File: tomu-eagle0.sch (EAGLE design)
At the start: 21 parts, among them U1 EFM32HG309F64G, X1 USBPCB

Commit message: added first pass at touch sensors
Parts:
- removed 0A, 0B, 1A, 1B: TPTP08R, testpad:TPTP08R
- removed X1: USBPCB, usb:USBPCB
- added U$1: USBPCB2, todstuff:USBPCB2
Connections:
- net CAP0A: no longer 0A.TP
- net CAP0B: no longer 0B.TP
- net CAP1A: no longer 1A.TP
- net CAP1B: no longer 1B.TP
- net GND: now also U$1.GND; no longer X1.GND
- net USB_D+: now also U$1.D+; no longer X1.D+
- net USB_D-: now also U$1.D-; no longer X1.D-
- net VUSB: now also U$1.VBUS; no longer X1.VBUS

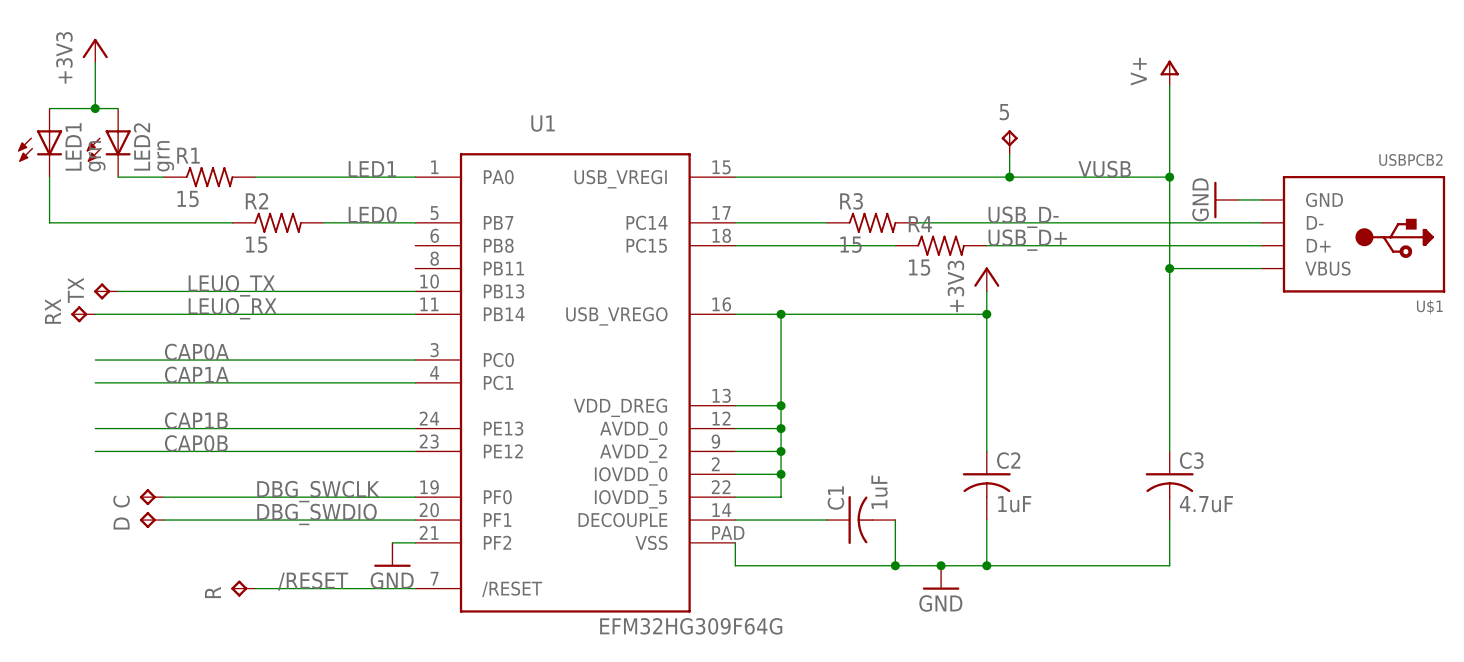
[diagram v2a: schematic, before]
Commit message: sigh. QFN24 is 5x5 not 4x4
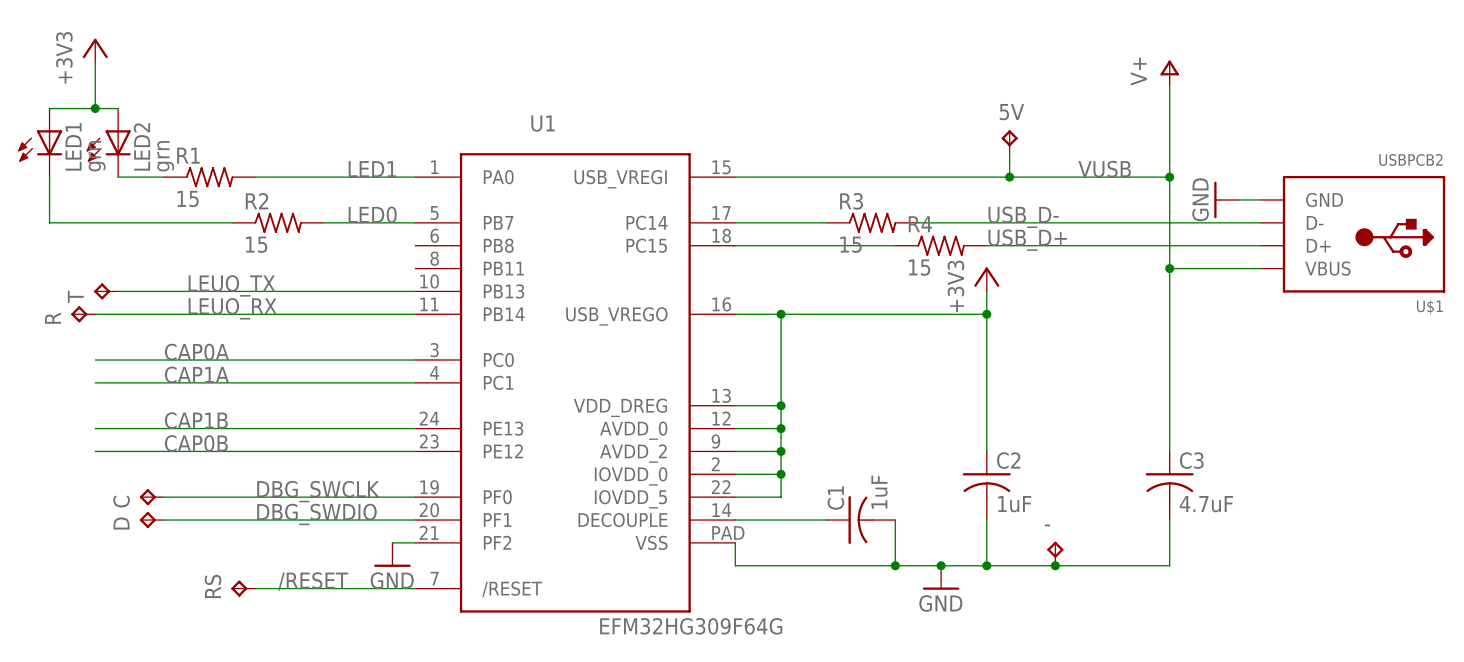
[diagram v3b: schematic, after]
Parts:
- removed RX, TX: TPTP08R, testpad:TPTP08R
- added -: TPTP10SQ, testpad:TPTP10SQ
- added RS, T: TPTP10R, testpad:TPTP10R
- C, D, R: value TPTP08R -> TPTP10R; device testpad:TPTP08R -> testpad:TPTP10R
- renumbered 5 to 5V
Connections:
- net /RESET: now also RS.TP; no longer R.TP
- net GND: now also -.TP
- net LEUO_RX: now also R.TP; no longer RX.TP
- net LEUO_TX: now also T.TP; no longer TX.TP
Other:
- moved on the sheet: R
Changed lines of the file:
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@@
 <part name="LED1" library="adafruit" library_urn="urn:adsk.eagle:library:420" deviceset="LED" device="CHIP-LED0603" value="grn"/>
 <part name="LED2" library="adafruit" library_urn="urn:adsk.eagle:library:420" deviceset="LED" device="CHIP-LED0603" value="grn"/>
-<part name="TX" library="testpad" library_urn="urn:adsk.eagle:library:385" deviceset="TP" device="TP08R" package3d_urn="urn:adsk.eagle:package:27956/1"/>
-<part name="RX" library="testpad" library_urn="urn:adsk.eagle:library:385" deviceset="TP" device="TP08R" package3d_urn="urn:adsk.eagle:package:27956/1"/>
-<part name="D" library="testpad" library_urn="urn:adsk.eagle:library:385" deviceset="TP" device="TP08R" package3d_urn="urn:adsk.eagle:package:27956/1"/>
-<part name="C" library="testpad" library_urn="urn:adsk.eagle:library:385" deviceset="TP" device="TP08R" package3d_urn="urn:adsk.eagle:package:27956/1"/>
-<part name="R" library="testpad" library_urn="urn:adsk.eagle:library:385" deviceset="TP" device="TP08R" package3d_urn="urn:adsk.eagle:package:27956/1"/>
+<part name="T" library="testpad" library_urn="urn:adsk.eagle:library:385" deviceset="TP" device="TP10R" package3d_urn="urn:adsk.eagle:package:27959/1" value="TPTP10R"/>
+<part name="R" library="testpad" library_urn="urn:adsk.eagle:library:385" deviceset="TP" device="TP10R" package3d_urn="urn:adsk.eagle:package:27959/1" value="TPTP10R"/>
+<part name="D" library="testpad" library_urn="urn:adsk.eagle:library:385" deviceset="TP" device="TP10R" package3d_urn="urn:adsk.eagle:package:27959/1" value="TPTP10R"/>
+<part name="C" library="testpad" library_urn="urn:adsk.eagle:library:385" deviceset="TP" device="TP10R" package3d_urn="urn:adsk.eagle:package:27959/1" value="TPTP10R"/>
+<part name="RS" library="testpad" library_urn="urn:adsk.eagle:library:385" deviceset="TP" device="TP10R" package3d_urn="urn:adsk.eagle:package:27959/1" value="TPTP10R"/>
 <part name="GND1" library="supply1" library_urn="urn:adsk.eagle:library:371" deviceset="GND" device=""/>
-<part name="5" library="testpad" library_urn="urn:adsk.eagle:library:385" deviceset="TP" device="TP08R" package3d_urn="urn:adsk.eagle:package:27956/1"/>
+<part name="5V" library="testpad" library_urn="urn:adsk.eagle:library:385" deviceset="TP" device="TP08R" package3d_urn="urn:adsk.eagle:package:27956/1"/>
 <part name="U$1" library="todstuff" deviceset="USB" device="PCB2"/>
+<part name="-" library="testpad" library_urn="urn:adsk.eagle:library:385" deviceset="TP" device="TP10SQ" package3d_urn="urn:adsk.eagle:package:27962/1" value="TPTP10SQ"/>
 </parts>
 <sheets>
@@
 <instance part="LED1" gate="G$1" x="12.7" y="76.2"/>
 <instance part="LED2" gate="G$1" x="20.32" y="76.2"/>
-<instance part="TX" gate="G$1" x="17.78" y="58.42" rot="R90"/>
-<instance part="RX" gate="G$1" x="15.24" y="55.88" rot="R90"/>
+<instance part="T" gate="G$1" x="17.78" y="58.42" rot="R90"/>
+<instance part="R" gate="G$1" x="15.24" y="55.88" rot="R90"/>
 <instance part="D" gate="G$1" x="22.86" y="33.02" rot="R90"/>
 <instance part="C" gate="G$1" x="22.86" y="35.56" rot="R90"/>
-<instance part="R" gate="G$1" x="33.02" y="25.4" rot="R90"/>
+<instance part="RS" gate="G$1" x="33.02" y="25.4" rot="R90"/>
 <instance part="GND1" gate="1" x="50.8" y="27.94"/>
-<instance part="5" gate="G$1" x="119.38" y="76.2"/>
+<instance part="5V" gate="G$1" x="119.38" y="76.2"/>
 <instance part="U$1" gate="G$1" x="154.94" y="63.5" rot="R180"/>
+<instance part="-" gate="G$1" x="124.46" y="30.48"/>
 </instances>
 <busses>
@@
 <pinref part="C2" gate="G$1" pin="2"/>
 <wire x1="116.84" y1="27.94" x2="116.84" y2="33.02" width="0.1524" layer="91"/>
-<wire x1="116.84" y1="27.94" x2="137.16" y2="27.94" width="0.1524" layer="91"/>
+<wire x1="116.84" y1="27.94" x2="124.46" y2="27.94" width="0.1524" layer="91"/>
 <junction x="116.84" y="27.94"/>
 <pinref part="C3" gate="G$1" pin="2"/>
+<wire x1="124.46" y1="27.94" x2="137.16" y2="27.94" width="0.1524" layer="91"/>
 <wire x1="137.16" y1="27.94" x2="137.16" y2="33.02" width="0.1524" layer="91"/>
+<pinref part="-" gate="G$1" pin="TP"/>
+<junction x="124.46" y="27.94"/>
 </segment>
 <segment>
@@
 <junction x="137.16" y="71.12"/>
 <label x="127" y="71.12" size="1.778" layer="95"/>
-<pinref part="5" gate="G$1" pin="TP"/>
+<pinref part="5V" gate="G$1" pin="TP"/>
 <wire x1="119.38" y1="71.12" x2="137.16" y2="71.12" width="0.1524" layer="91"/>
 <wire x1="119.38" y1="73.66" x2="119.38" y2="71.12" width="0.1524" layer="91"/>
@@
 <pinref part="U1" gate="G$1" pin="PB13"/>
 <wire x1="53.34" y1="58.42" x2="20.32" y2="58.42" width="0.1524" layer="91"/>
-<pinref part="TX" gate="G$1" pin="TP"/>
+<pinref part="T" gate="G$1" pin="TP"/>
 <label x="27.94" y="58.42" size="1.778" layer="95"/>
 </segment>
@@
 <pinref part="U1" gate="G$1" pin="PB14"/>
 <wire x1="53.34" y1="55.88" x2="17.78" y2="55.88" width="0.1524" layer="91"/>
-<pinref part="RX" gate="G$1" pin="TP"/>
+<pinref part="R" gate="G$1" pin="TP"/>
 <label x="27.94" y="55.88" size="1.778" layer="95"/>
 </segment>
@@
 <wire x1="53.34" y1="25.4" x2="35.56" y2="25.4" width="0.1524" layer="91"/>
 <label x="38.1" y="25.4" size="1.778" layer="95"/>
-<pinref part="R" gate="G$1" pin="TP"/>
-</segment>
-</net>
+<pinref part="RS" gate="G$1" pin="TP"/>
+</segment>
+</net>

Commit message: more fixes
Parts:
- 5V: value TPTP08R -> TPTP10R; device testpad:TPTP08R -> testpad:TPTP10R
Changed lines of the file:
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@@
 <?xml version="1.0" encoding="utf-8"?>
 <!DOCTYPE eagle SYSTEM "eagle.dtd">
-<eagle version="8.5.2">
+<eagle version="8.6.0">
 <drawing>
 <settings>
@@
 <grid distance="0.1" unitdist="inch" unit="inch" style="lines" multiple="1" display="no" altdistance="0.01" altunitdist="inch" altunit="inch"/>
 <layers>
-<layer number="1" name="Top" color="4" fill="1" visible="no" active="no"/>
-<layer number="2" name="Route2" color="1" fill="3" visible="no" active="no"/>
-<layer number="3" name="Route3" color="4" fill="3" visible="no" active="no"/>
-<layer number="4" name="Route4" color="1" fill="4" visible="no" active="no"/>
-<layer number="5" name="Route5" color="4" fill="4" visible="no" active="no"/>
-<layer number="6" name="Route6" color="1" fill="8" visible="no" active="no"/>
-<layer number="7" name="Route7" color="4" fill="8" visible="no" active="no"/>
-<layer number="8" name="Route8" color="1" fill="2" visible="no" active="no"/>
-<layer number="9" name="Route9" color="4" fill="2" visible="no" active="no"/>
-<layer number="10" name="Route10" color="1" fill="7" visible="no" active="no"/>
-<layer number="11" name="Route11" color="4" fill="7" visible="no" active="no"/>
-<layer number="12" name="Route12" color="1" fill="5" visible="no" active="no"/>
-<layer number="13" name="Route13" color="4" fill="5" visible="no" active="no"/>
-<layer number="14" name="Route14" color="1" fill="6" visible="no" active="no"/>
-<layer number="15" name="Route15" color="4" fill="6" visible="no" active="no"/>
-<layer number="16" name="Bottom" color="3" fill="1" visible="no" active="no"/>
-<layer number="17" name="Pads" color="2" fill="1" visible="no" active="no"/>
-<layer number="18" name="Vias" color="2" fill="1" visible="no" active="no"/>
-<layer number="19" name="Unrouted" color="6" fill="1" visible="no" active="no"/>
-<layer number="20" name="Dimension" color="15" fill="1" visible="no" active="no"/>
-<layer number="21" name="tPlace" color="7" fill="1" visible="no" active="no"/>
-<layer number="22" name="bPlace" color="7" fill="1" visible="no" active="no"/>
-<layer number="23" name="tOrigins" color="15" fill="1" visible="no" active="no"/>
-<layer number="24" name="bOrigins" color="15" fill="1" visible="no" active="no"/>
-<layer number="25" name="tNames" color="7" fill="1" visible="no" active="no"/>
-<layer number="26" name="bNames" color="7" fill="1" visible="no" active="no"/>
-<layer number="27" name="tValues" color="7" fill="1" visible="no" active="no"/>
-<layer number="28" name="bValues" color="7" fill="1" visible="no" active="no"/>
+<layer number="1" name="Top" color="4" fill="1" visible="yes" active="no"/>
+<layer number="2" name="Route2" color="1" fill="3" visible="yes" active="no"/>
+<layer number="3" name="Route3" color="4" fill="3" visible="yes" active="no"/>
+<layer number="4" name="Route4" color="1" fill="4" visible="yes" active="no"/>
+<layer number="5" name="Route5" color="4" fill="4" visible="yes" active="no"/>
+<layer number="6" name="Route6" color="1" fill="8" visible="yes" active="no"/>
+<layer number="7" name="Route7" color="4" fill="8" visible="yes" active="no"/>
+<layer number="8" name="Route8" color="1" fill="2" visible="yes" active="no"/>
+<layer number="9" name="Route9" color="4" fill="2" visible="yes" active="no"/>
+<layer number="10" name="Route10" color="1" fill="7" visible="yes" active="no"/>
+<layer number="11" name="Route11" color="4" fill="7" visible="yes" active="no"/>
+<layer number="12" name="Route12" color="1" fill="5" visible="yes" active="no"/>
+<layer number="13" name="Route13" color="4" fill="5" visible="yes" active="no"/>
+<layer number="14" name="Route14" color="1" fill="6" visible="yes" active="no"/>
+<layer number="15" name="Route15" color="4" fill="6" visible="yes" active="no"/>
+<layer number="16" name="Bottom" color="3" fill="1" visible="yes" active="no"/>
+<layer number="17" name="Pads" color="2" fill="1" visible="yes" active="no"/>
+<layer number="18" name="Vias" color="2" fill="1" visible="yes" active="no"/>
+<layer number="19" name="Unrouted" color="6" fill="1" visible="yes" active="no"/>
+<layer number="20" name="Dimension" color="15" fill="1" visible="yes" active="no"/>
+<layer number="21" name="tPlace" color="7" fill="1" visible="yes" active="no"/>
+<layer number="22" name="bPlace" color="7" fill="1" visible="yes" active="no"/>
+<layer number="23" name="tOrigins" color="15" fill="1" visible="yes" active="no"/>
+<layer number="24" name="bOrigins" color="15" fill="1" visible="yes" active="no"/>
+<layer number="25" name="tNames" color="7" fill="1" visible="yes" active="no"/>
+<layer number="26" name="bNames" color="7" fill="1" visible="yes" active="no"/>
+<layer number="27" name="tValues" color="7" fill="1" visible="yes" active="no"/>
+<layer number="28" name="bValues" color="7" fill="1" visible="yes" active="no"/>
 <layer number="29" name="tStop" color="7" fill="3" visible="no" active="no"/>
 <layer number="30" name="bStop" color="7" fill="6" visible="no" active="no"/>
@@
 <layer number="35" name="tGlue" color="7" fill="4" visible="no" active="no"/>
 <layer number="36" name="bGlue" color="7" fill="5" visible="no" active="no"/>
-<layer number="37" name="tTest" color="7" fill="1" visible="no" active="no"/>
-<layer number="38" name="bTest" color="7" fill="1" visible="no" active="no"/>
+<layer number="37" name="tTest" color="7" fill="1" visible="yes" active="no"/>
+<layer number="38" name="bTest" color="7" fill="1" visible="yes" active="no"/>
 <layer number="39" name="tKeepout" color="4" fill="11" visible="no" active="no"/>
 <layer number="40" name="bKeepout" color="1" fill="11" visible="no" active="no"/>
@@
 <layer number="44" name="Drills" color="7" fill="1" visible="no" active="no"/>
 <layer number="45" name="Holes" color="7" fill="1" visible="no" active="no"/>
-<layer number="46" name="Milling" color="3" fill="1" visible="no" active="no"/>
-<layer number="47" name="Measures" color="7" fill="1" visible="no" active="no"/>
-<layer number="48" name="Document" color="7" fill="1" visible="no" active="no"/>
-<layer number="49" name="Reference" color="7" fill="1" visible="no" active="no"/>
-<layer number="50" name="dxf" color="7" fill="1" visible="no" active="no"/>
-<layer number="51" name="tDocu" color="7" fill="1" visible="no" active="no"/>
-<layer number="52" name="bDocu" color="7" fill="1" visible="no" active="no"/>
-<layer number="53" name="tGND_GNDA" color="7" fill="9" visible="no" active="no"/>
-<layer number="54" name="bGND_GNDA" color="1" fill="9" visible="no" active="no"/>
-<layer number="56" name="wert" color="7" fill="1" visible="no" active="no"/>
-<layer number="57" name="tCAD" color="7" fill="1" visible="no" active="no"/>
-<layer number="59" name="tCarbon" color="7" fill="1" visible="no" active="no"/>
-<layer number="60" name="bCarbon" color="7" fill="1" visible="no" active="no"/>
+<layer number="46" name="Milling" color="3" fill="1" visible="yes" active="no"/>
+<layer number="47" name="Measures" color="7" fill="1" visible="yes" active="no"/>
+<layer number="48" name="Document" color="7" fill="1" visible="yes" active="no"/>
+<layer number="49" name="Reference" color="7" fill="1" visible="yes" active="no"/>
+<layer number="50" name="dxf" color="7" fill="1" visible="yes" active="no"/>
+<layer number="51" name="tDocu" color="7" fill="1" visible="yes" active="no"/>
+<layer number="52" name="bDocu" color="7" fill="1" visible="yes" active="no"/>
+<layer number="53" name="tGND_GNDA" color="7" fill="9" visible="yes" active="no"/>
+<layer number="54" name="bGND_GNDA" color="1" fill="9" visible="yes" active="no"/>
+<layer number="56" name="wert" color="7" fill="1" visible="yes" active="no"/>
+<layer number="57" name="tCAD" color="7" fill="1" visible="yes" active="no"/>
+<layer number="59" name="tCarbon" color="7" fill="1" visible="yes" active="no"/>
+<layer number="60" name="bCarbon" color="7" fill="1" visible="yes" active="no"/>
 <layer number="88" name="SimResults" color="9" fill="1" visible="yes" active="yes"/>
 <layer number="89" name="SimProbes" color="9" fill="1" visible="yes" active="yes"/>
@@
 <part name="RS" library="testpad" library_urn="urn:adsk.eagle:library:385" deviceset="TP" device="TP10R" package3d_urn="urn:adsk.eagle:package:27959/1" value="TPTP10R"/>
 <part name="GND1" library="supply1" library_urn="urn:adsk.eagle:library:371" deviceset="GND" device=""/>
-<part name="5V" library="testpad" library_urn="urn:adsk.eagle:library:385" deviceset="TP" device="TP08R" package3d_urn="urn:adsk.eagle:package:27956/1"/>
+<part name="5V" library="testpad" library_urn="urn:adsk.eagle:library:385" deviceset="TP" device="TP10R" package3d_urn="urn:adsk.eagle:package:27959/1" value="TPTP10R"/>
 <part name="U$1" library="todstuff" deviceset="USB" device="PCB2"/>
 <part name="-" library="testpad" library_urn="urn:adsk.eagle:library:385" deviceset="TP" device="TP10SQ" package3d_urn="urn:adsk.eagle:package:27962/1" value="TPTP10SQ"/>
